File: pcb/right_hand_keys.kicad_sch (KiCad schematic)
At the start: 35 parts, among them U0 SW_Push

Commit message: Label parts for JLCPCB
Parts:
- D_{AS}2, D_{AS}3, D_{B}0, D_{D}0, D_{E}0, D_{F}0, D_{G}0, D_{L}0, D_{NUM}1, D_{PR}0, D_{RR}0, D_{S}2, D_{TR}0, D_{U}0, D_{Z}0: LCSC (none) -> C78740
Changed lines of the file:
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@@
 			)
 		)
+		(property "LCSC" "C78740"
+			(at 167.64 80.01 0)
+			(effects
+				(font
+					(size 1.27 1.27)
+				)
+				(hide yes)
+			)
+		)
 		(pin "2"
 		)
@@
 			)
 		)
+		(property "LCSC" "C78740"
+			(at 167.64 101.6 0)
+			(effects
+				(font
+					(size 1.27 1.27)
+				)
+				(hide yes)
+			)
+		)
 		(pin "2"
 		)
@@
 			)
 		)
+		(property "LCSC" "C78740"
+			(at 127 101.6 0)
+			(effects
+				(font
+					(size 1.27 1.27)
+				)
+				(hide yes)
+			)
+		)
 		(pin "2"
 		)
@@
 			)
 		)
+		(property "LCSC" "C78740"
+			(at 46.99 80.01 0)
+			(effects
+				(font
+					(size 1.27 1.27)
+				)
+				(hide yes)
+			)
+		)
 		(pin "2"
 		)
@@
 			)
 		)
+		(property "LCSC" "C78740"
+			(at 248.92 101.6 0)
+			(effects
+				(font
+					(size 1.27 1.27)
+				)
+				(hide yes)
+			)
+		)
 		(pin "2"
 		)
@@
 			)
 		)
+		(property "LCSC" "C78740"
+			(at 46.99 101.6 0)
+			(effects
+				(font
+					(size 1.27 1.27)
+				)
+				(hide yes)
+			)
+		)
 		(pin "2"
 		)
@@
 			)
 		)
+		(property "LCSC" "C78740"
+			(at 248.92 80.01 0)
+			(effects
+				(font
+					(size 1.27 1.27)
+				)
+				(hide yes)
+			)
+		)
 		(pin "2"
 		)
@@
 			)
 		)
+		(property "LCSC" "C78740"
+			(at 86.36 123.19 0)
+			(effects
+				(font
+					(size 1.27 1.27)
+				)
+				(hide yes)
+			)
+		)
 		(pin "2"
 		)
@@
 			)
 		)
+		(property "LCSC" "C78740"
+			(at 208.28 101.6 0)
+			(effects
+				(font
+					(size 1.27 1.27)
+				)
+				(hide yes)
+			)
+		)
 		(pin "2"
 		)
@@
 			)
 		)
+		(property "LCSC" "C78740"
+			(at 127 80.01 0)
+			(effects
+				(font
+					(size 1.27 1.27)
+				)
+				(hide yes)
+			)
+		)
 		(pin "2"
 		)
@@
 			)
 		)
+		(property "LCSC" "C78740"
+			(at 86.36 80.01 0)
+			(effects
+				(font
+					(size 1.27 1.27)
+				)
+				(hide yes)
+			)
+		)
 		(pin "2"
 		)
@@
 			)
 		)
+		(property "LCSC" "C78740"
+			(at 208.28 80.01 0)
+			(effects
+				(font
+					(size 1.27 1.27)
+				)
+				(hide yes)
+			)
+		)
 		(pin "2"
 		)
@@
 			)
 		)
+		(property "LCSC" "C78740"
+			(at 46.99 123.19 0)
+			(effects
+				(font
+					(size 1.27 1.27)
+				)
+				(hide yes)
+			)
+		)
 		(pin "2"
 		)
@@
 			)
 		)
+		(property "LCSC" "C78740"
+			(at 124.46 48.26 0)
+			(effects
+				(font
+					(size 1.27 1.27)
+				)
+				(hide yes)
+			)
+		)
 		(pin "2"
 		)
@@
 			(at 86.36 101.6 0)
 			(effects
+				(font
+					(size 1.27 1.27)
+				)
+				(hide yes)
+			)
+		)
+		(property "LCSC" "C78740"
+			(at 86.36 101.6 0)
+			(effects

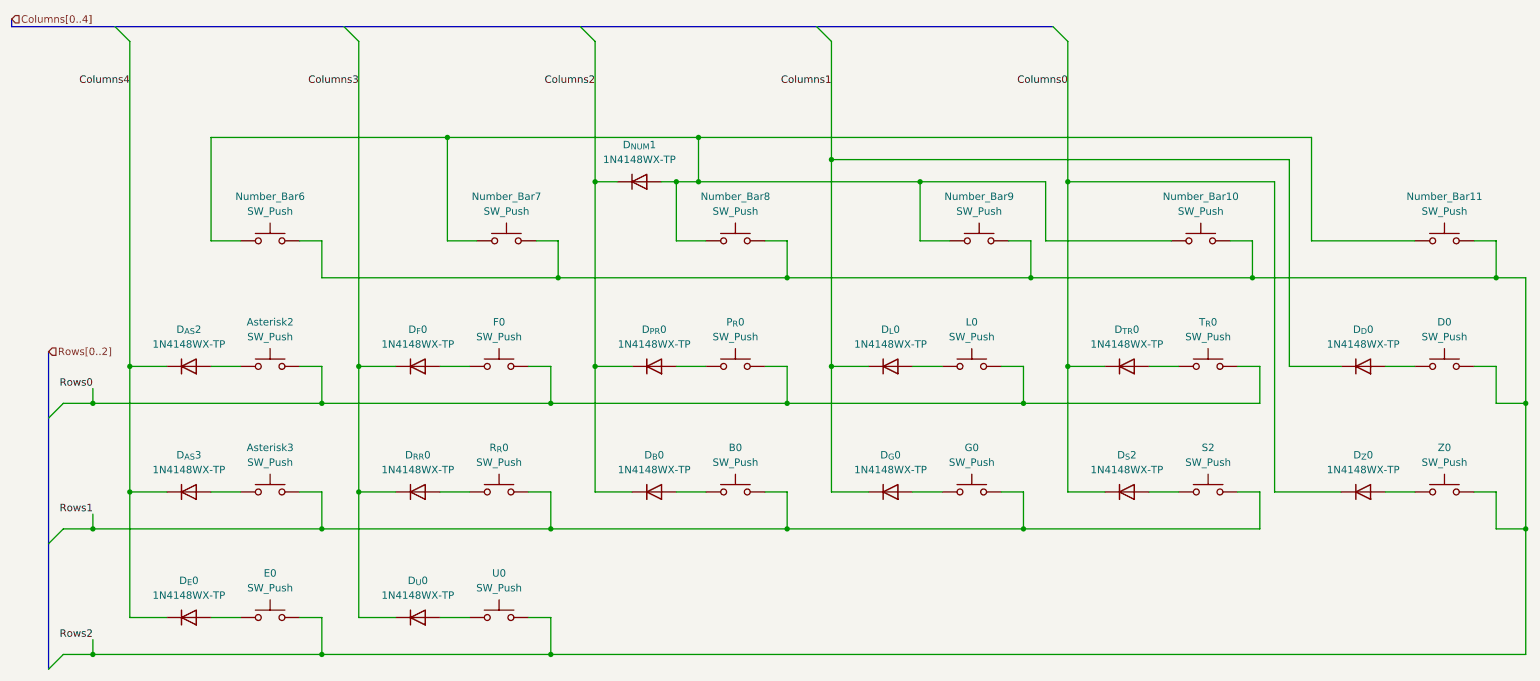
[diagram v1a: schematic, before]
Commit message: Add DNP for right hand
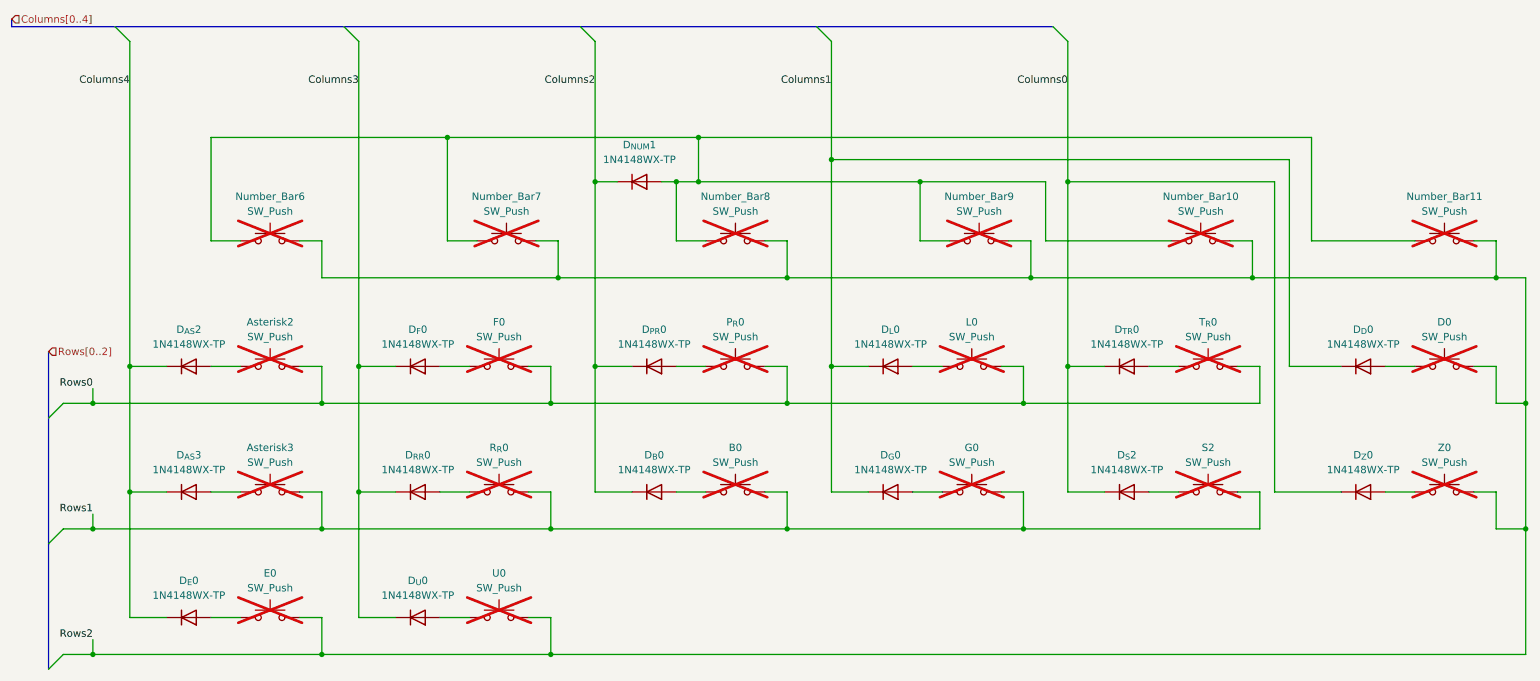
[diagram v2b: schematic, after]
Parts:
- Asterisk2, Asterisk3, B0, D0, E0, F0, G0, L0, Number_Bar10, Number_Bar11, Number_Bar6, Number_Bar7, Number_Bar8, Number_Bar9, P_{R}0, R_{R}0, S2, T_{R}0, U0, Z0: now not fitted
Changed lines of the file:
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@@
 		(in_bom yes)
 		(on_board yes)
-		(dnp no)
+		(dnp yes)
 		(fields_autoplaced yes)
 		(property "Reference" "Number_Bar6"
@@
 		(in_bom yes)
 		(on_board yes)
-		(dnp no)
+		(dnp yes)
 		(property "Reference" "U0"
 			(at 100.33 115.57 0)
@@
 		(in_bom yes)
 		(on_board yes)
-		(dnp no)
+		(dnp yes)
 		(property "Reference" "Z0"
 			(at 262.89 93.98 0)
@@
 		(in_bom yes)
 		(on_board yes)
-		(dnp no)
+		(dnp yes)
 		(fields_autoplaced yes)
 		(property "Reference" "Number_Bar7"
@@
 		(in_bom yes)
 		(on_board yes)
-		(dnp no)
+		(dnp yes)
 		(property "Reference" "E0"
 			(at 60.96 115.57 0)
@@
 		(in_bom yes)
 		(on_board yes)
-		(dnp no)
+		(dnp yes)
 		(property "Reference" "T_{R}0"
 			(at 222.25 72.39 0)
@@
 		(in_bom yes)
 		(on_board yes)
-		(dnp no)
+		(dnp yes)
 		(property "Reference" "L0"
 			(at 181.61 72.39 0)
@@
 		(in_bom yes)
 		(on_board yes)
-		(dnp no)
+		(dnp yes)
 		(property "Reference" "G0"
 			(at 181.61 93.98 0)
@@
 		(in_bom yes)
 		(on_board yes)
-		(dnp no)
+		(dnp yes)
 		(property "Reference" "B0"
 			(at 140.97 93.98 0)
@@
 		(in_bom yes)
 		(on_board yes)
-		(dnp no)
+		(dnp yes)
 		(property "Reference" "Asterisk2"
 			(at 60.96 72.39 0)
@@
 		(in_bom yes)
 		(on_board yes)
-		(dnp no)
+		(dnp yes)
 		(fields_autoplaced yes)
 		(property "Reference" "Number_Bar10"
@@
 		(in_bom yes)
 		(on_board yes)
-		(dnp no)
+		(dnp yes)
 		(property "Reference" "D0"
 			(at 262.89 72.39 0)
@@
 		(in_bom yes)
 		(on_board yes)
-		(dnp no)
+		(dnp yes)
 		(property "Reference" "R_{R}0"
 			(at 100.33 93.98 0)
@@
 		(in_bom yes)
 		(on_board yes)
-		(dnp no)
+		(dnp yes)
 		(property "Reference" "F0"
 			(at 100.33 72.39 0)
@@
 		(in_bom yes)
 		(on_board yes)
-		(dnp no)
+		(dnp yes)
 		(property "Reference" "Asterisk3"
 			(at 60.96 93.98 0)
@@
 		(in_bom yes)
 		(on_board yes)
-		(dnp no)
+		(dnp yes)
 		(property "Reference" "P_{R}0"
 			(at 140.97 72.39 0)
@@
 		(in_bom yes)
 		(on_board yes)
-		(dnp no)
+		(dnp yes)
 		(fields_autoplaced yes)
 		(property "Reference" "Number_Bar8"
@@
 		(in_bom yes)
 		(on_board yes)
-		(dnp no)
+		(dnp yes)
 		(property "Reference" "S2"
 			(at 222.25 93.98 0)
@@
 		(in_bom yes)
 		(on_board yes)
-		(dnp no)
+		(dnp yes)
 		(fields_autoplaced yes)
 		(property "Reference" "Number_Bar9"
@@
 		(in_bom yes)
 		(on_board yes)
-		(dnp no)
+		(dnp yes)
 		(fields_autoplaced yes)
 		(property "Reference" "Number_Bar11"
